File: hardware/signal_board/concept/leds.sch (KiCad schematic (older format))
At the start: 4 parts

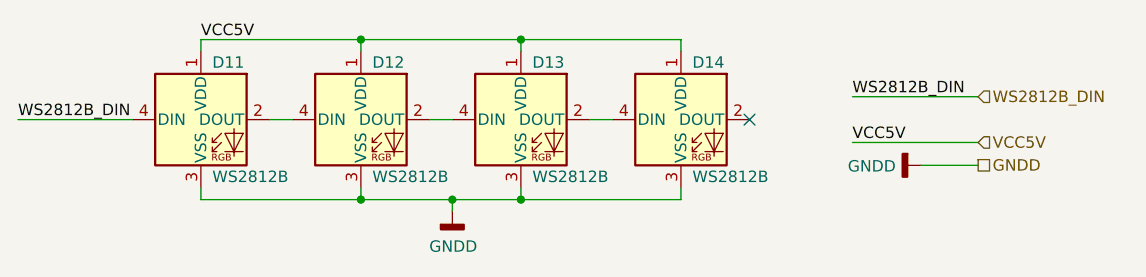
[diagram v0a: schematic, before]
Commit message: Add priduction board
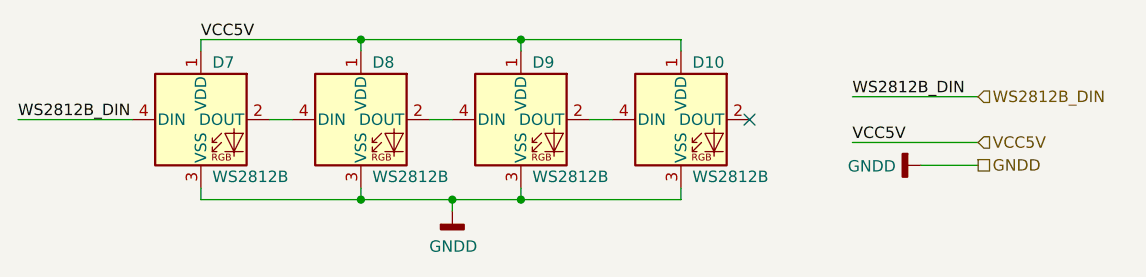
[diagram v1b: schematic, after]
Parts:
- renumbered D14 to D10, D11 to D7, D12 to D8, D13 to D9
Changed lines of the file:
@@
 $Descr A4 11693 8268
 encoding utf-8
-Sheet 6 12
+Sheet 9 16
 Title ""
 Date ""
@@
 $EndDescr
 $Comp
-L LED:WS2812B D11
+L LED:WS2812B D7
 U 1 1 5E9BEE64
 P 4200 3950
-F 0 "D11" H 4250 4200 50  0000 L CNN
+F 0 "D7" H 4250 4200 50  0000 L CNN
 F 1 "WS2812B" H 4250 3700 50  0000 L CNN
 F 2 "LED_SMD:LED_WS2812B_PLCC4_5.0x5.0mm_P3.2mm" H 4250 3650 50  0001 L TNN
@@
 $EndComp
 $Comp
-L LED:WS2812B D12
+L LED:WS2812B D8
 U 1 1 5E9BF639
 P 4900 3950
-F 0 "D12" H 4950 4200 50  0000 L CNN
+F 0 "D8" H 4950 4200 50  0000 L CNN
 F 1 "WS2812B" H 4950 3700 50  0000 L CNN
 F 2 "LED_SMD:LED_WS2812B_PLCC4_5.0x5.0mm_P3.2mm" H 4950 3650 50  0001 L TNN
@@
 $EndComp
 $Comp
-L LED:WS2812B D13
+L LED:WS2812B D9
 U 1 1 5E9C0F86
 P 5600 3950
-F 0 "D13" H 5650 4200 50  0000 L CNN
+F 0 "D9" H 5650 4200 50  0000 L CNN
 F 1 "WS2812B" H 5650 3700 50  0000 L CNN
 F 2 "LED_SMD:LED_WS2812B_PLCC4_5.0x5.0mm_P3.2mm" H 5650 3650 50  0001 L TNN
@@
 $EndComp
 $Comp
-L LED:WS2812B D14
+L LED:WS2812B D10
 U 1 1 5E9C0F8C
 P 6300 3950
-F 0 "D14" H 6350 4200 50  0000 L CNN
+F 0 "D10" H 6350 4200 50  0000 L CNN
 F 1 "WS2812B" H 6350 3700 50  0000 L CNN
 F 2 "LED_SMD:LED_WS2812B_PLCC4_5.0x5.0mm_P3.2mm" H 6350 3650 50  0001 L TNN
@@
 VCC5V
 $Comp
-L power:GNDD #PWR070
+L power:GNDD #PWR063
 U 1 1 5EACFEC6
 P 5300 4350
-F 0 "#PWR070" H 5300 4100 50  0001 C CNN
+F 0 "#PWR063" H 5300 4100 50  0001 C CNN
 F 1 "GNDD" H 5304 4195 50  0000 C CNN
 F 2 "" H 5300 4350 50  0001 C CNN
@@
 VCC5V
 $Comp
-L power:GNDD #PWR071
+L power:GNDD #PWR064
 U 1 1 5EAE9AE7
 P 7350 4150
-F 0 "#PWR071" H 7350 3900 50  0001 C CNN
+F 0 "#PWR064" H 7350 3900 50  0001 C CNN
 F 1 "GNDD" V 7354 4040 50  0000 R CNN
 F 2 "" H 7350 4150 50  0001 C CNN
